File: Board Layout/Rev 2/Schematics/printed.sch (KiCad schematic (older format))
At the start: 5 parts, among them P1 CONN_5X2

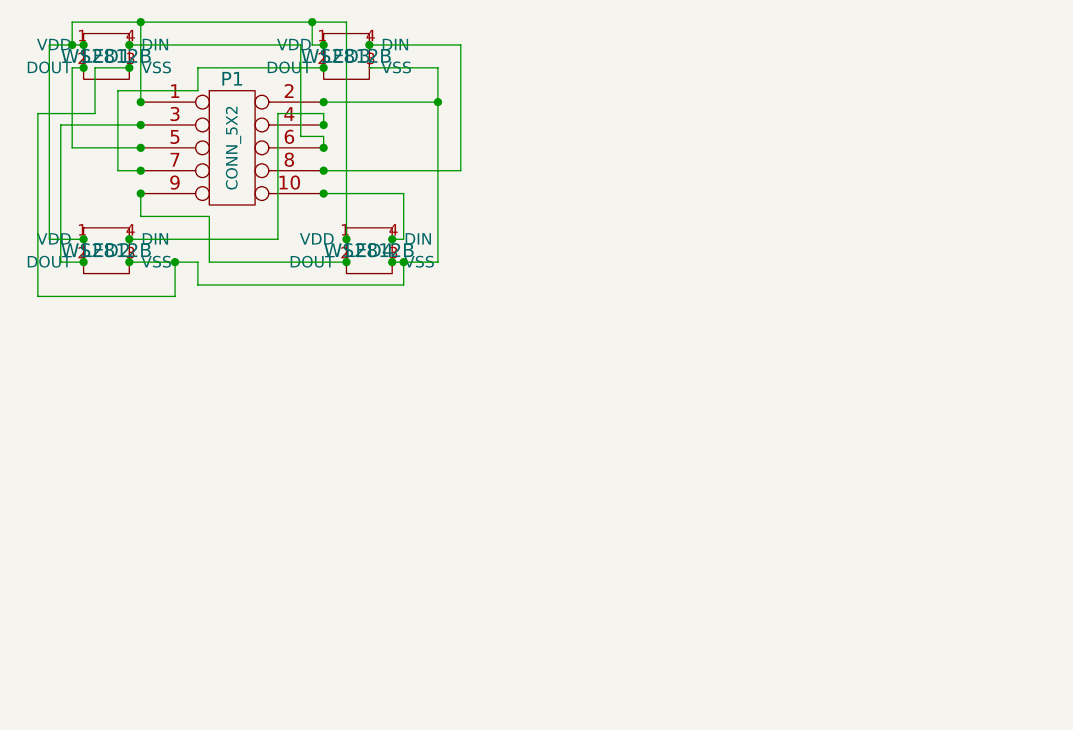
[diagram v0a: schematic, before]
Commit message: Board Update
not sure if I can do 2 layer as it is too condensed. Might need to
switch to 4 layer.
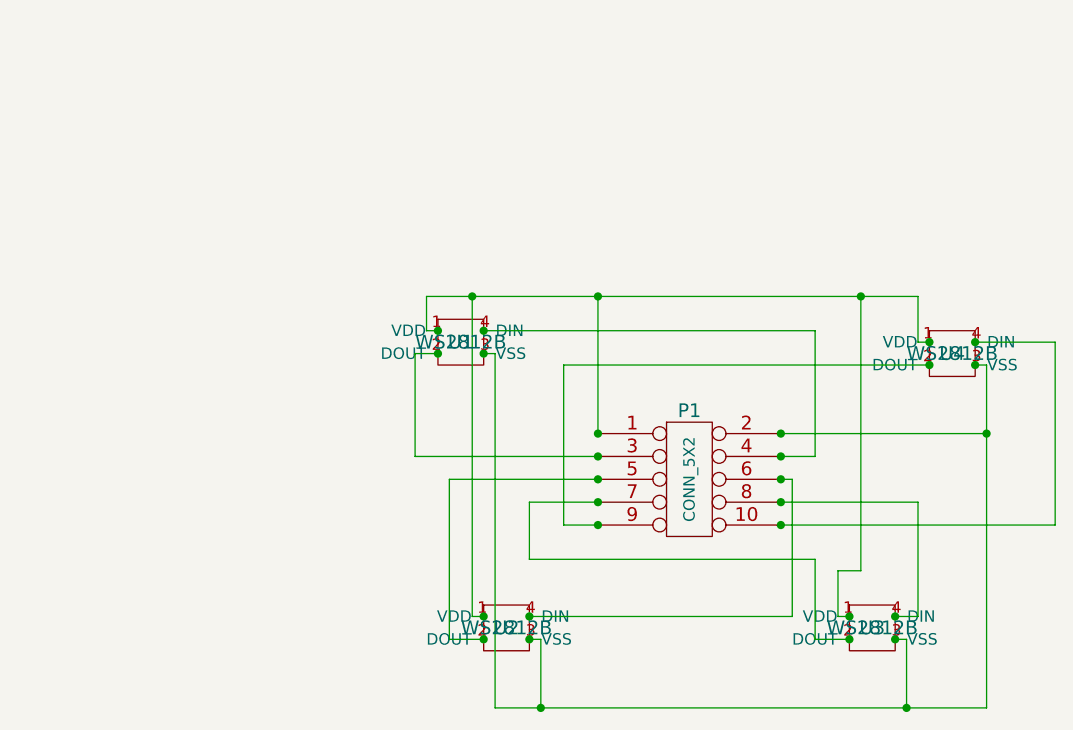
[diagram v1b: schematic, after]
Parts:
- removed LED1, LED2, LED3, LED4: WS2812B, ~, symbol WS2812B
- added U1, U2, U3, U4: WS2812B, ~, symbol WS2812B
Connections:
- net at P1.1: now also U1.1 (VDD), U2.1 (VDD), U3.1 (VDD), U4.1 (VDD)
- net at P1.5: now also U2.2 (DOUT)
- net at P1.2: now also U1.3 (VSS), U2.3 (VSS), U3.3 (VSS), U4.3 (VSS)
- net at P1.6: now also U2.4 (DIN)
- net at P1.7: now also U3.2 (DOUT)
- net at P1.8: now also U3.4 (DIN)
- net at P1.3: now also U1.2 (DOUT)
- net at P1.4: now also U1.4 (DIN)
- net at P1.9: now also U4.2 (DOUT)
- net at P1.10: now also U4.4 (DIN)
